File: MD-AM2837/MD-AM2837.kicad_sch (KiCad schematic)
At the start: 13 parts, among them J1 XT60_Male_Horizontal, J2 XT60_Female_Horizontal, J3 Conn_01x03_Pin_signal

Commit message: v0.1
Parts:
- added D1, D2: 1N4007, Diode_THT:D_DO-41_SOD81_P10.16mm_Horizontal, symbol Diode:1N4007
- added LED4: PWR, LED_SMD:LED_0603_1608Metric_Pad1.05x0.95mm_HandSolder, symbol 00_mylib:LED1608
- added Q1, Q2: BSS138, Package_TO_SOT_SMD:SOT-23, symbol Transistor_FET:BSS138
- added R4: R10k, Resistor_SMD:R_0603_1608Metric_Pad0.98x0.95mm_HandSolder, symbol 00_mylib:R1608
- C1: footprint Capacitor_SMD:C_Elec_10x10.2 -> Capacitor_THT:C_Radial_D8.0mm_H11.5mm_P3.50mm
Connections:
- net GND: now also Q1.2 (S), Q2.2 (S), R4.2
- net IN_A: now reaches J3.1 (Pin_1), MD1.1 (IN_A)
- net IN_A: now also Q1.1 (G); no longer R1.2
- net IN_B: now reaches J3.2 (Pin_2), MD1.2 (IN_B)
- net IN_B: now also Q2.1 (G); no longer R2.2
- net OUT_A: now reaches C3.1, J2.2 (VOUT), MD1.7 (OUT_A), MD1.8 (OUT_A)
- net OUT_A: now also D1.2 (A)
- net OUT_B: now reaches C3.2, J2.1 (GND), MD1.5 (OUT_B), MD1.6 (OUT_B)
- net OUT_B: now also D2.2 (A)
- new net: Q2.3 (D), R2.2
- new net: D1.1 (K), D2.1 (K), LED4.2 (A)
- new net: LED4.1 (K), R4.1
- new net: Q1.3 (D), R1.2
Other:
- moved on the sheet: LED1, LED2, R1, R2

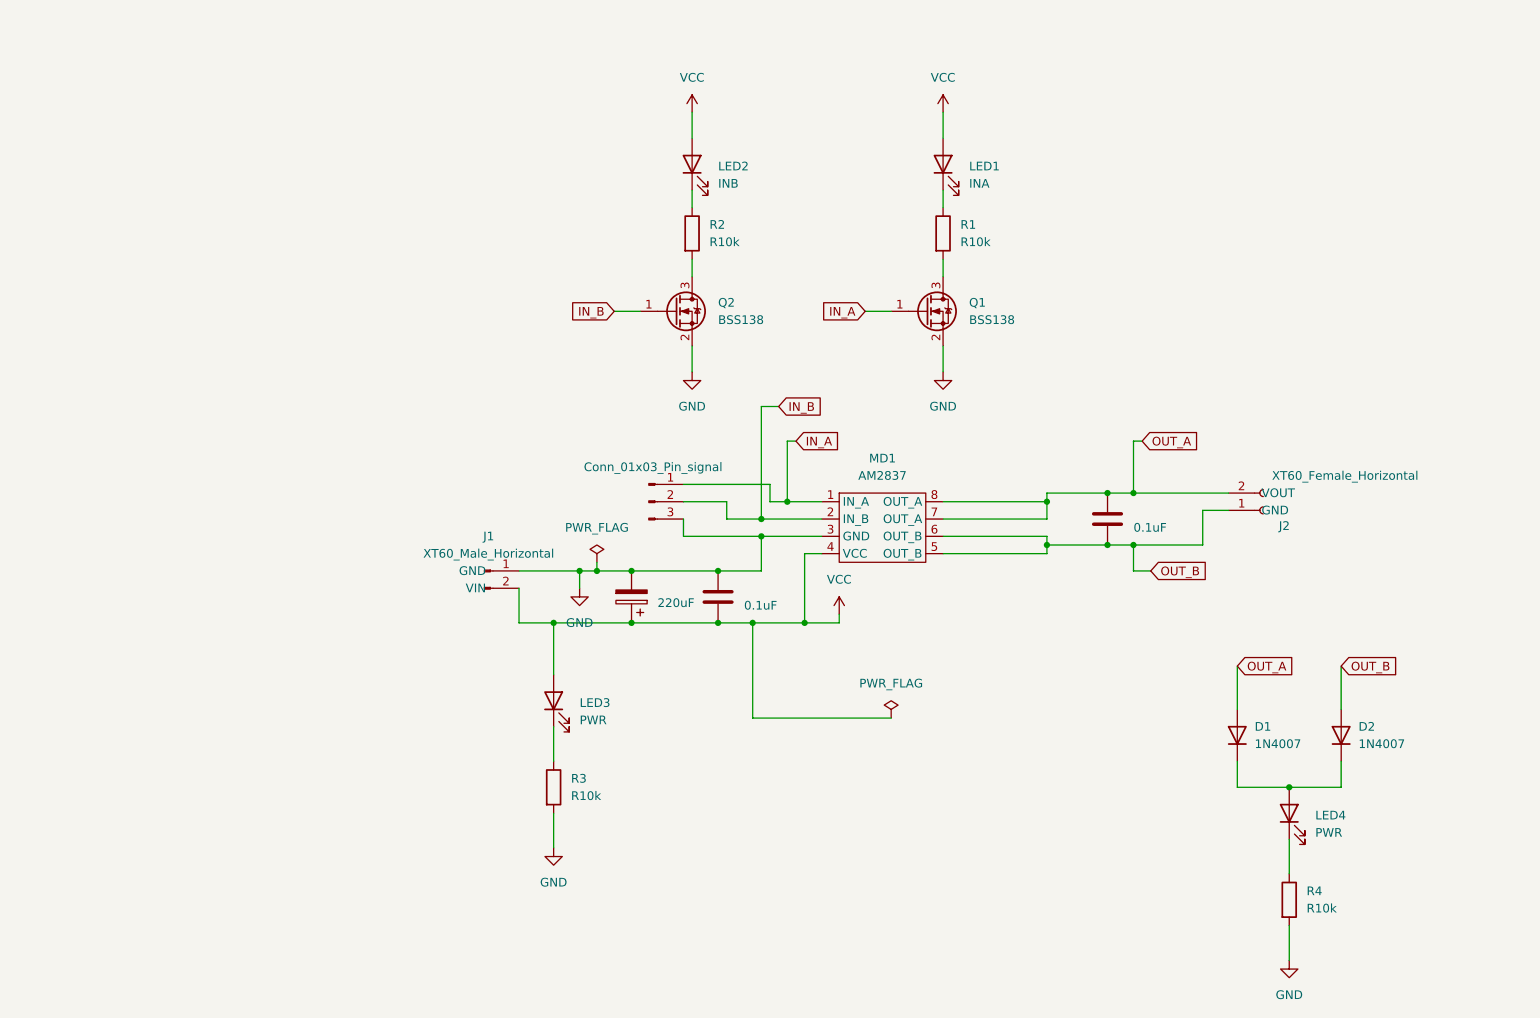
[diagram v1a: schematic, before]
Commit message: フォトカプラ追加中
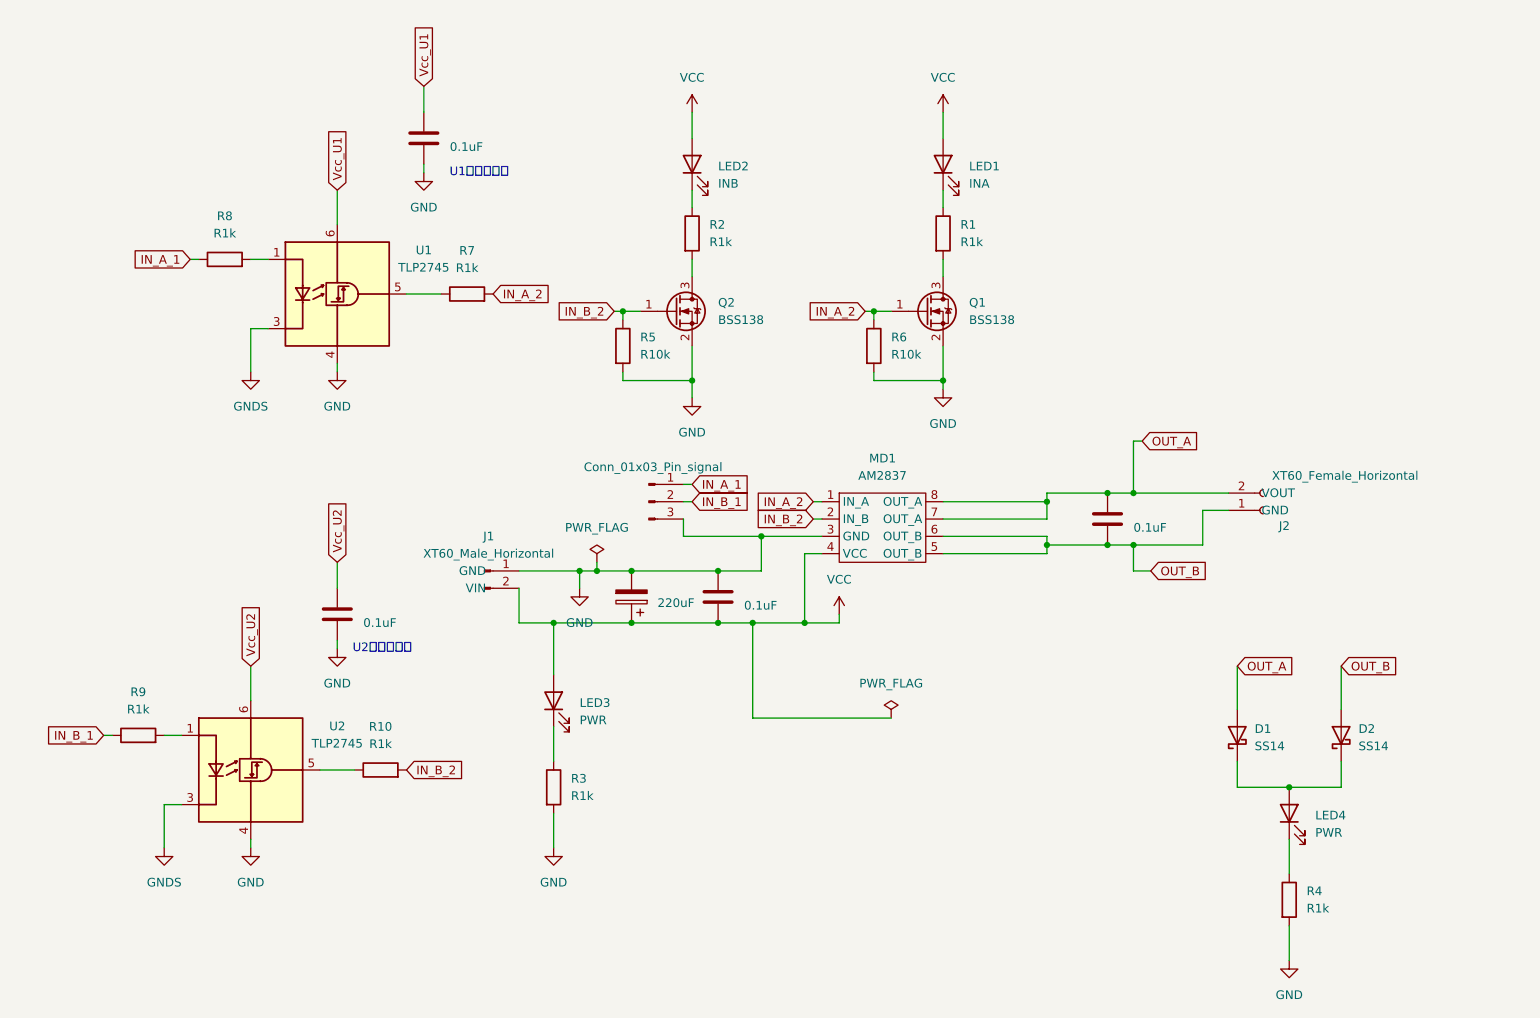
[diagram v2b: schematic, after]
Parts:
- removed D1, D2: 1N4007, Diode_THT:D_DO-41_SOD81_P10.16mm_Horizontal, symbol Diode:1N4007
- added C4, C5: 0.1uF, Capacitor_SMD:C_0603_1608Metric_Pad1.08x0.95mm_HandSolder, symbol 00_mylib:C1608
- added D1, D2: SS14, Diode_SMD:D_SMA, symbol Diode:SS14
- added R10, R7, R8, R9: R1k, Resistor_SMD:R_0603_1608Metric_Pad0.98x0.95mm_HandSolder, symbol 00_mylib:R1608
- added R5, R6: R10k, Resistor_SMD:R_0603_1608Metric_Pad0.98x0.95mm_HandSolder, symbol 00_mylib:R1608
- added U1, U2: TLP2745, Package_SO:SO-6L_10x3.84mm_P1.27mm, symbol Isolator:TLP2745
- R1, R2, R3, R4: value R10k -> R1k
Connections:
- net GND: now also C4.2, C5.2, R5.2, R6.2, U1.4 (GND), U2.4 (GND)
- net OUT_A: now also D1.2 (A)
- net OUT_B: now also D2.2 (A)
- net at LED4.2 (A): now also D1.1 (K), D2.1 (K)
- net IN_A renamed IN_A_2
- net IN_A_2: now also R6.1, R7.2; no longer J3.1 (Pin_1)
- net IN_B renamed IN_B_2
- net IN_B_2: now also R10.2, R5.1; no longer J3.2 (Pin_2)
- new net: R8.2, U1.1 (A)
- new net: R7.1, U1.5 (VO)
- new net: R10.1, U2.5 (VO)
- new net: R9.2, U2.1 (A)
- new net GNDS: U1.3 (K), U2.3 (K)
- new net IN_A_1: J3.1 (Pin_1), R8.1
- new net IN_B_1: J3.2 (Pin_2), R9.1
- new net Vcc_U1: C4.1, U1.6 (VDD)
- new net Vcc_U2: C5.1, U2.6 (VDD)
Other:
- note added: "U1に近づける"
- note added: "U2に近づける"

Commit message: v0.2作成
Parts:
- C1: value 220uF -> 220
- C2, C3, C4, C5: value 0.1uF -> 0.1
- R1, R10, R2, R3, R4, R7: value R1k -> 1k
- R5, R6: value R10k -> 10k
- R8, R9: value R1k -> 10
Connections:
- net GND: no longer J3.3 (Pin_3)
- net GNDS: now also J3.3 (Pin_3)
- net IN_A_2: now also R7.1, U1.5 (VO); no longer Q1.1 (G), R6.1, R7.2
- net IN_B_2: now also R10.1, U2.5 (VO); no longer Q2.1 (G), R10.2, R5.1
- new net: Q2.1 (G), R10.2, R5.1
- new net: Q1.1 (G), R6.1, R7.2
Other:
- moved on the sheet: LED1, Q1, R1, R10, R6, R7, R8, U1
